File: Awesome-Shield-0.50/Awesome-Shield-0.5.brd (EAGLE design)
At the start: 51 x 55 mm, 37 parts, among them J2 ARDUINO_R3_SHIELD, SW1 SPST_TACT-EVQQ2, U1 LIGHTSENSORTEMT6000

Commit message: rm thermistor
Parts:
- removed F1: PTCTHERMISTOR1206, SparkFun-PowerIC:PTC-1206
- removed R12: 10K Ohm, rcl:R0603
- removed R7: 10K Ohm, rcl:R1206
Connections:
- removed net A2: F1.2, J2.A2, R12.1, R7.1
- net GND: no longer F1.1
- net IOREF: no longer R12.2, R7.2
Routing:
- net A2: track 44.5 -> 0.00 mm, vias 2 -> 0
- net GND: track 18.5 -> 4.48 mm
- net IOREF: track 53.8 -> 49.6 mm
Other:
- board text removed: "temp"
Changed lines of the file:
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@@
 <text x="77.96" y="65.304" size="2.54" layer="21" font="vector" rot="R270">button</text>
 <text x="76.01" y="44.498" size="2.54" layer="21" font="vector" rot="R270">knob</text>
-<text x="80.396" y="27.064" size="2.54" layer="21" font="vector" rot="R90">temp</text>
 <text x="67.032" y="32.126" size="2.54" layer="21" font="vector" rot="R270">light</text>
 <text x="51.436" y="22.508" size="2.54" layer="21" font="vector" rot="R90">port1</text>
@@
 <wire x1="61" y1="60.5" x2="61" y2="65" width="0.254" layer="21"/>
 <wire x1="61" y1="65" x2="60.5" y2="65" width="0.254" layer="21"/>
-<rectangle x1="73.152" y1="25.4" x2="81.28" y2="35.56" layer="41"/>
-<rectangle x1="74.676" y1="25.908" x2="81.28" y2="36.068" layer="42"/>
 </plain>
 <attributes>
@@
 </autorouter>
 <elements>
-<element name="F1" library="SparkFun-PowerIC" package="PTC-1206" value="PTCTHERMISTOR1206" x="76.5" y="30.5" smashed="yes" rot="R90">
-<attribute name="PROD_ID" value="RES-08585" x="76.5" y="30.5" size="1.778" layer="27" rot="R90" display="off"/>
-</element>
 <element name="LED1" library="adafruit" package="RGBLED5050" value="RGBLED5050" x="48" y="54" smashed="yes" rot="R180"/>
 <element name="R1" library="rcl" package="R1206" value="130 Ohm" x="57.5" y="62" smashed="yes" rot="R180"/>
@@
 <element name="R3" library="rcl" package="R1206" value="130 Ohm" x="57.5" y="53.55" smashed="yes" rot="R180"/>
 <element name="R6" library="rcl" package="R1206" value="10K" x="57.5" y="34.5" smashed="yes" rot="R180"/>
-<element name="R7" library="rcl" package="R1206" value="10K Ohm" x="57.5" y="39" smashed="yes"/>
 <element name="SW1" library="adafruit" package="EVQ-Q2" value="SPST_TACT-EVQQ2" x="71" y="61" smashed="yes" rot="R180"/>
 <element name="SG1" library="SparkFun-Electromechanical" package="BUZZER-CCV" value="BUZZERSMD2" x="43" y="40.5" rot="R180"/>
@@
 <element name="R10" library="rcl" package="R0603" value="130 Ohm" x="58" y="58.3" smashed="yes"/>
 <element name="R11" library="rcl" package="R0603" value="10K" x="58" y="36.5" smashed="yes"/>
-<element name="R12" library="rcl" package="R0603" value="10K Ohm" x="58" y="41.5" smashed="yes"/>
 <element name="J3" library="Seeed-OPL-Connector" package="HW4-SMD-2.0" value="" x="42" y="25" smashed="yes">
 <attribute name="VALUE" x="40.095" y="27.413" size="0.889" layer="27" font="vector" ratio="11"/>
@@
 </signal>
 <signal name="GND">
-<contactref element="F1" pad="1"/>
 <contactref element="LED1" pad="4"/>
 <contactref element="LED1" pad="6"/>
@@
 <via x="33.5" y="56.5" extent="1-16" drill="0.6" diameter="1.15"/>
 <via x="64" y="20.5" extent="1-16" drill="0.6" diameter="1.27"/>
-<wire x1="76.5" y1="28.625" x2="78.409" y2="28.625" width="0.4064" layer="1"/>
-<wire x1="78.409" y1="28.625" x2="78.74" y2="28.956" width="0.4064" layer="1"/>
-<wire x1="78.74" y1="28.956" x2="78.74" y2="36.068" width="0.4064" layer="1"/>
-<wire x1="78.74" y1="36.068" x2="77.724" y2="37.084" width="0.4064" layer="1"/>
-<wire x1="77.724" y1="37.084" x2="74.676" y2="37.084" width="0.4064" layer="1"/>
 <wire x1="57.15" y1="35.572" x2="57.15" y2="36.5" width="0.4064" layer="1"/>
-</signal>
-<signal name="A2">
-<contactref element="R7" pad="1"/>
-<contactref element="F1" pad="2"/>
-<contactref element="R12" pad="1"/>
-<contactref element="J2" pad="A2"/>
-<wire x1="57.15" y1="41.5" x2="57.15" y2="40.072" width="0.4064" layer="1"/>
-<wire x1="76.5" y1="32.375" x2="73.375" y2="32.375" width="0.4064" layer="1"/>
-<wire x1="73.375" y1="32.375" x2="72.5" y2="31.5" width="0.4064" layer="1"/>
-<via x="72.5" y="31.5" extent="1-16" drill="0.6" diameter="1.27"/>
-<wire x1="72.5" y1="31.5" x2="72.5" y2="36.5" width="0.4064" layer="16"/>
-<wire x1="72.5" y1="36.5" x2="70" y2="39" width="0.4064" layer="16"/>
-<wire x1="70" y1="39" x2="67" y2="39" width="0.4064" layer="16"/>
-<wire x1="67" y1="39" x2="64.5" y2="41.5" width="0.4064" layer="16"/>
-<wire x1="64.5" y1="41.5" x2="55.5" y2="41.5" width="0.4064" layer="16"/>
-<via x="55.5" y="41.5" extent="1-16" drill="0.6" diameter="1.27"/>
-<wire x1="55.5" y1="41.5" x2="57.15" y2="41.5" width="0.4064" layer="1"/>
-<wire x1="71.605" y1="20.37" x2="71.605" y2="30.605" width="0.4064" layer="16"/>
-<wire x1="71.605" y1="30.605" x2="72.5" y2="31.5" width="0.4064" layer="16"/>
-<wire x1="57.15" y1="40.072" x2="56.078" y2="39" width="0.4064" layer="1"/>
 </signal>
 <signal name="N$3">
@@
 </signal>
 <signal name="IOREF">
-<contactref element="R7" pad="2"/>
-<contactref element="R12" pad="2"/>
 <contactref element="RV1" pad="P$3"/>
 <contactref element="J2" pad="IOREF"/>
@@
 <wire x1="70" y1="42" x2="74.5" y2="42" width="0.8128" layer="1"/>
 <wire x1="63" y1="39" x2="60.5" y2="39" width="0.8128" layer="1"/>
-<wire x1="60.5" y1="39" x2="58.922" y2="39" width="0.4064" layer="1"/>
 <wire x1="70" y1="42" x2="69" y2="41" width="0.8128" layer="1"/>
 <wire x1="69" y1="41" x2="67" y2="41" width="0.8128" layer="1"/>
@@
 <wire x1="64.99" y1="28.71" x2="63.79" y2="28.71" width="0.4064" layer="1"/>
 <wire x1="63.79" y1="28.71" x2="61.71" y2="28.71" width="0.8128" layer="1"/>
-<wire x1="58.922" y1="39" x2="58.85" y2="39" width="0.4064" layer="1"/>
-<wire x1="58.85" y1="39" x2="58.85" y2="41.5" width="0.4064" layer="1"/>
 </signal>
 <signal name="+3V3">

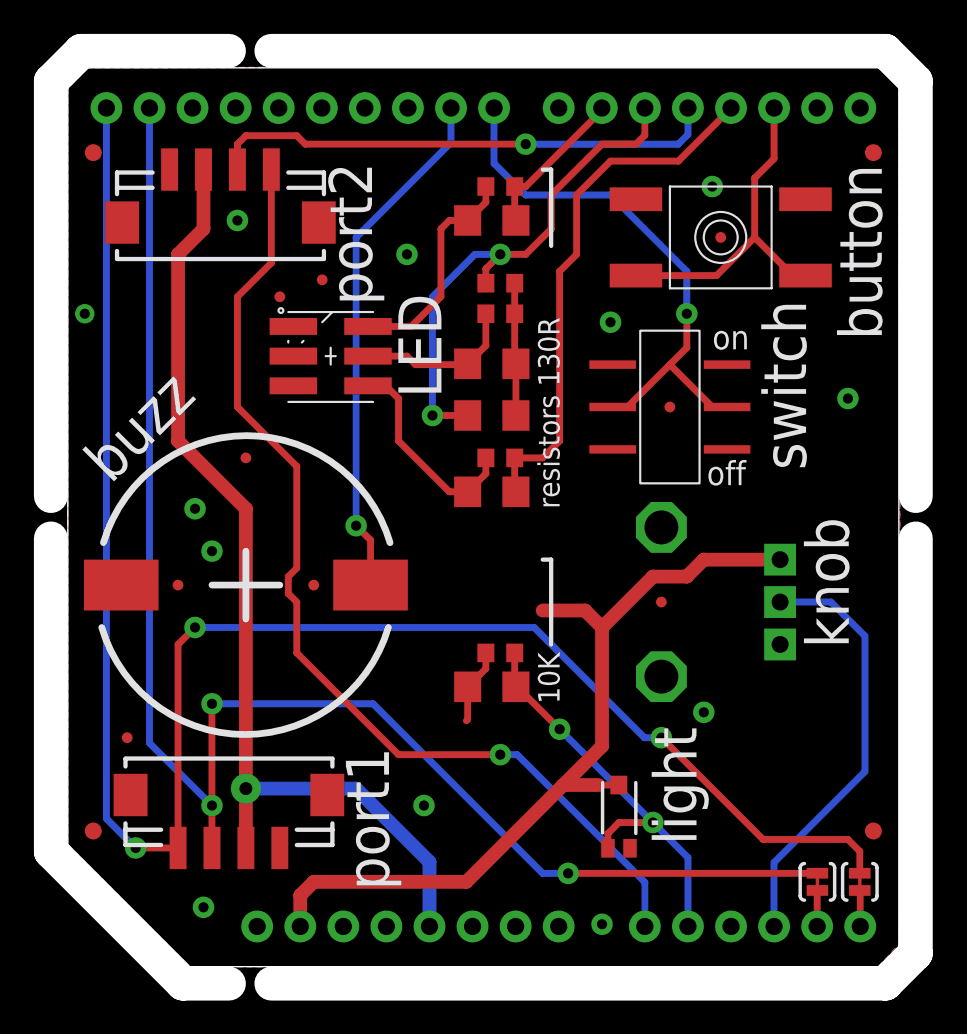
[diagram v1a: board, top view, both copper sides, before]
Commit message: swapped out shield part for headers
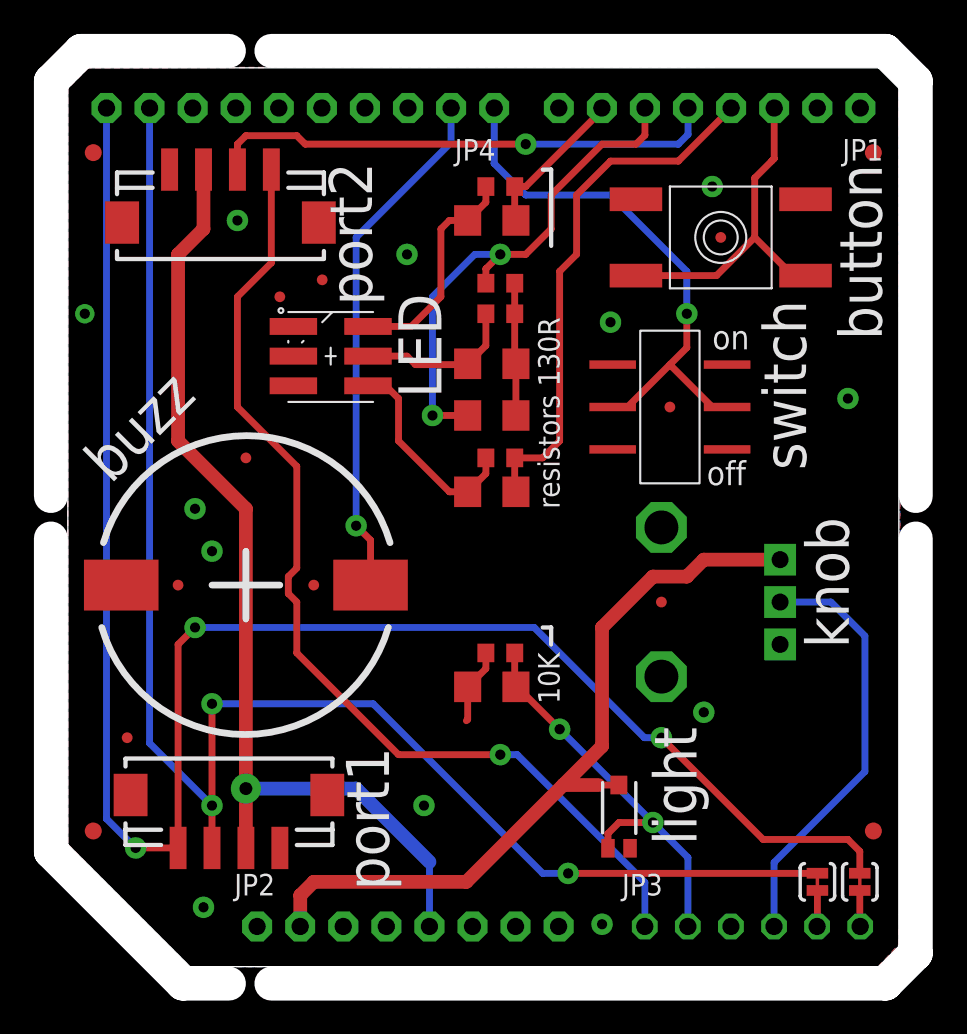
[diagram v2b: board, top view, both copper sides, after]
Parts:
- removed J2: ARDUINO_R3_SHIELD, SparkFun-Boards:UNO_R3_SHIELD
- added JP1, JP2: (no value), adafruit:1X08-CLEANBIG
- added JP3: (no value), adafruit:1X06-CLEAN
- added JP4: PINHD-1X10, adafruit:1X10-BIG
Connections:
- new net A2: JP3.3
- new net AREF: JP4.8
- new net D10: JP4.3
- new net D11: JP4.4
- new net D12: JP4.5
- new net D13: JP4.6
- new net D7: JP1.8
- new net N$39: JP2.1
- new net RES: JP2.3
- new net RX: JP1.1
- new net TX: JP1.2
- new net VIN: JP2.8
- net +3V3: now also JP2.4; no longer J2.3.3V
- net +5V: now also JP2.5; no longer J2.5V
- net A0: now also JP3.1; no longer J2.A0
- net A1: now also JP3.2; no longer J2.A1
- net A3: now also JP3.4; no longer J2.A3
- net A4: now also JP3.5; no longer J2.A4
- net A5: now also JP3.6; no longer J2.A5
- net D2: now also JP1.3; no longer J2.D2
- net D3: now also JP1.4; no longer J2.D3
- net D4: now also JP1.5; no longer J2.D4
- net D5: now also JP1.6; no longer J2.D5
- net D6: now also JP1.7; no longer J2.D6
- net D8: now also JP4.1; no longer J2.D8
- net D9: now also JP4.2; no longer J2.D9
- net GND: now also JP2.6, JP2.7, JP4.7; no longer J2.GND@0, J2.GND@1, J2.GND@2
- net IOREF: now also JP2.2; no longer J2.IOREF
- net SCL: now also JP4.10; no longer J2.SCL
- net SDA: now also JP4.9; no longer J2.SDA
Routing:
- net IOREF: track 49.6 -> 45.7 mm

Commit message: adjusted sch to make refdes more visible
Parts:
- renumbered S2 to SW2
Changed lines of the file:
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@@
 <element name="SJ1" library="SparkFun-Passives" package="PAD-JUMPER-2-NC_BY_TRACE_YES_SILK" value="JUMPER-PAD-2-NC_BY_TRACE" x="76.7" y="23" smashed="yes" rot="R270"/>
 <element name="SJ2" library="SparkFun-Passives" package="PAD-JUMPER-2-NC_BY_TRACE_YES_SILK" value="JUMPER-PAD-2-NC_BY_TRACE" x="79.2" y="23" smashed="yes" rot="R270"/>
-<element name="S2" library="SparkFun-Electromechanical" package="AYZ0202" value="DPDT" x="68" y="51" smashed="yes" rot="R90">
+<element name="SW2" library="SparkFun-Electromechanical" package="AYZ0202" value="DPDT" x="68" y="51" smashed="yes" rot="R90">
 <attribute name="PROD_ID" value="SWCH-08179" x="68" y="51" size="1.778" layer="27" rot="R90" display="off"/>
 </element>
@@
 <contactref element="SW1" pad="A"/>
 <contactref element="SW1" pad="A'"/>
-<contactref element="S2" pad="6"/>
-<contactref element="S2" pad="3"/>
+<contactref element="SW2" pad="6"/>
+<contactref element="SW2" pad="3"/>
 <contactref element="SG1" pad="+"/>
 <polygon width="0.4064" layer="1" isolate="0.4064">
@@
 <signal name="N$3">
 <contactref element="R3" pad="2"/>
-<contactref element="LED1" pad="2"/>
 <contactref element="R9" pad="2"/>
-<wire x1="50.2" y1="54" x2="52.5" y2="54" width="0.4064" layer="1"/>
 <wire x1="52.5" y1="54" x2="53" y2="53.5" width="0.4064" layer="1"/>
 <wire x1="53" y1="53.5" x2="56.028" y2="53.5" width="0.4064" layer="1"/>
@@
 <wire x1="57.15" y1="56.5" x2="57.15" y2="54.622" width="0.4064" layer="1"/>
 <wire x1="57.15" y1="54.622" x2="56.078" y2="53.55" width="0.4064" layer="1"/>
+<contactref element="LED1" pad="2"/>
+<wire x1="52.5" y1="54" x2="50.2" y2="54" width="0.4064" layer="1"/>
 </signal>
 <signal name="D2">
@@
 </signal>
 <signal name="D8">
-<contactref element="S2" pad="2"/>
-<contactref element="S2" pad="5"/>
+<contactref element="SW2" pad="2"/>
+<contactref element="SW2" pad="5"/>
 <wire x1="57.635" y1="65.365" x2="59.5" y2="63.5" width="0.4064" layer="16"/>
 <wire x1="59.5" y1="63.5" x2="64.5" y2="63.5" width="0.4064" layer="16"/>
@@
 </signal>
 <signal name="N$8">
-<contactref element="LED1" pad="3"/>
 <contactref element="R8" pad="2"/>
 <contactref element="R1" pad="2"/>
-<wire x1="50.2" y1="55.75" x2="52.75" y2="55.75" width="0.4064" layer="1"/>
 <wire x1="52.75" y1="55.75" x2="54.5" y2="57.5" width="0.4064" layer="1"/>
 <wire x1="54.5" y1="57.5" x2="54.5" y2="61.5" width="0.4064" layer="1"/>
@@
 <wire x1="57.15" y1="64" x2="57.15" y2="63.072" width="0.4064" layer="1"/>
 <wire x1="57.15" y1="63.072" x2="56.078" y2="62" width="0.4064" layer="1"/>
+<contactref element="LED1" pad="3"/>
+<wire x1="52.75" y1="55.75" x2="50.2" y2="55.75" width="0.4064" layer="1"/>
 </signal>
 <signal name="D3">
